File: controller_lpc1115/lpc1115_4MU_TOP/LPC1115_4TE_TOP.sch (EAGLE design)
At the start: 102 parts, among them P2 ISP, Q1 BC856, Q2 BCP52, Q3 BC847C, U1 LPC1115FBD48, U2 BD9G101, U3 XO32 12MHz

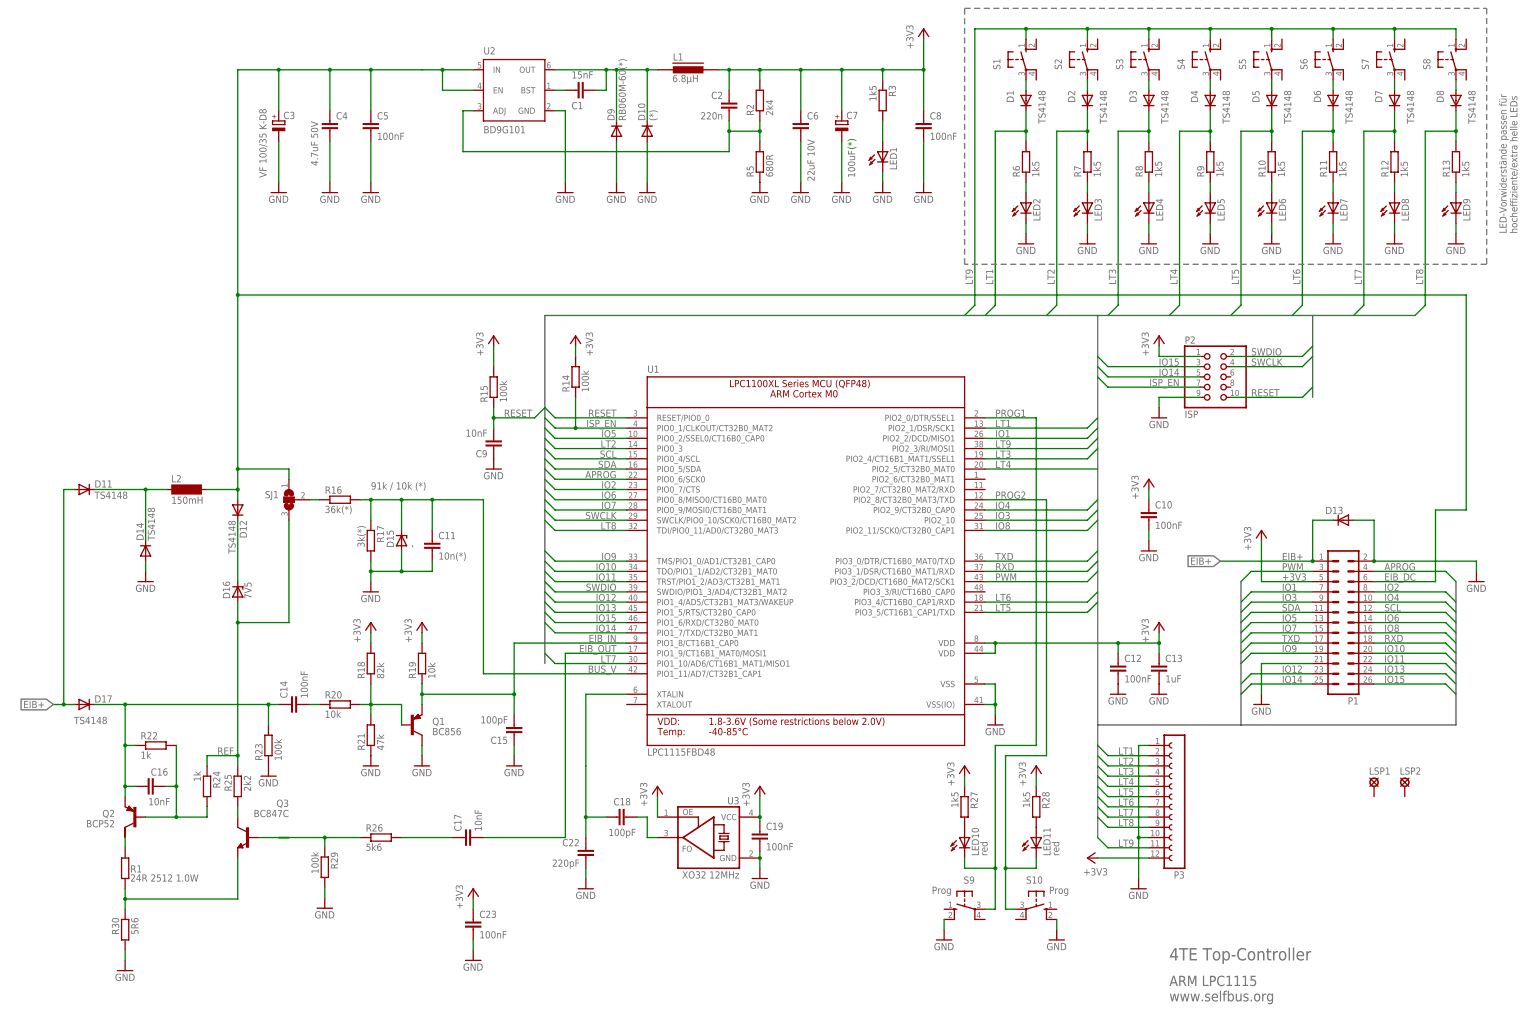
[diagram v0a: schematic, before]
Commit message: [ctrl_4MU_TOP] - intermediate status of re-routing
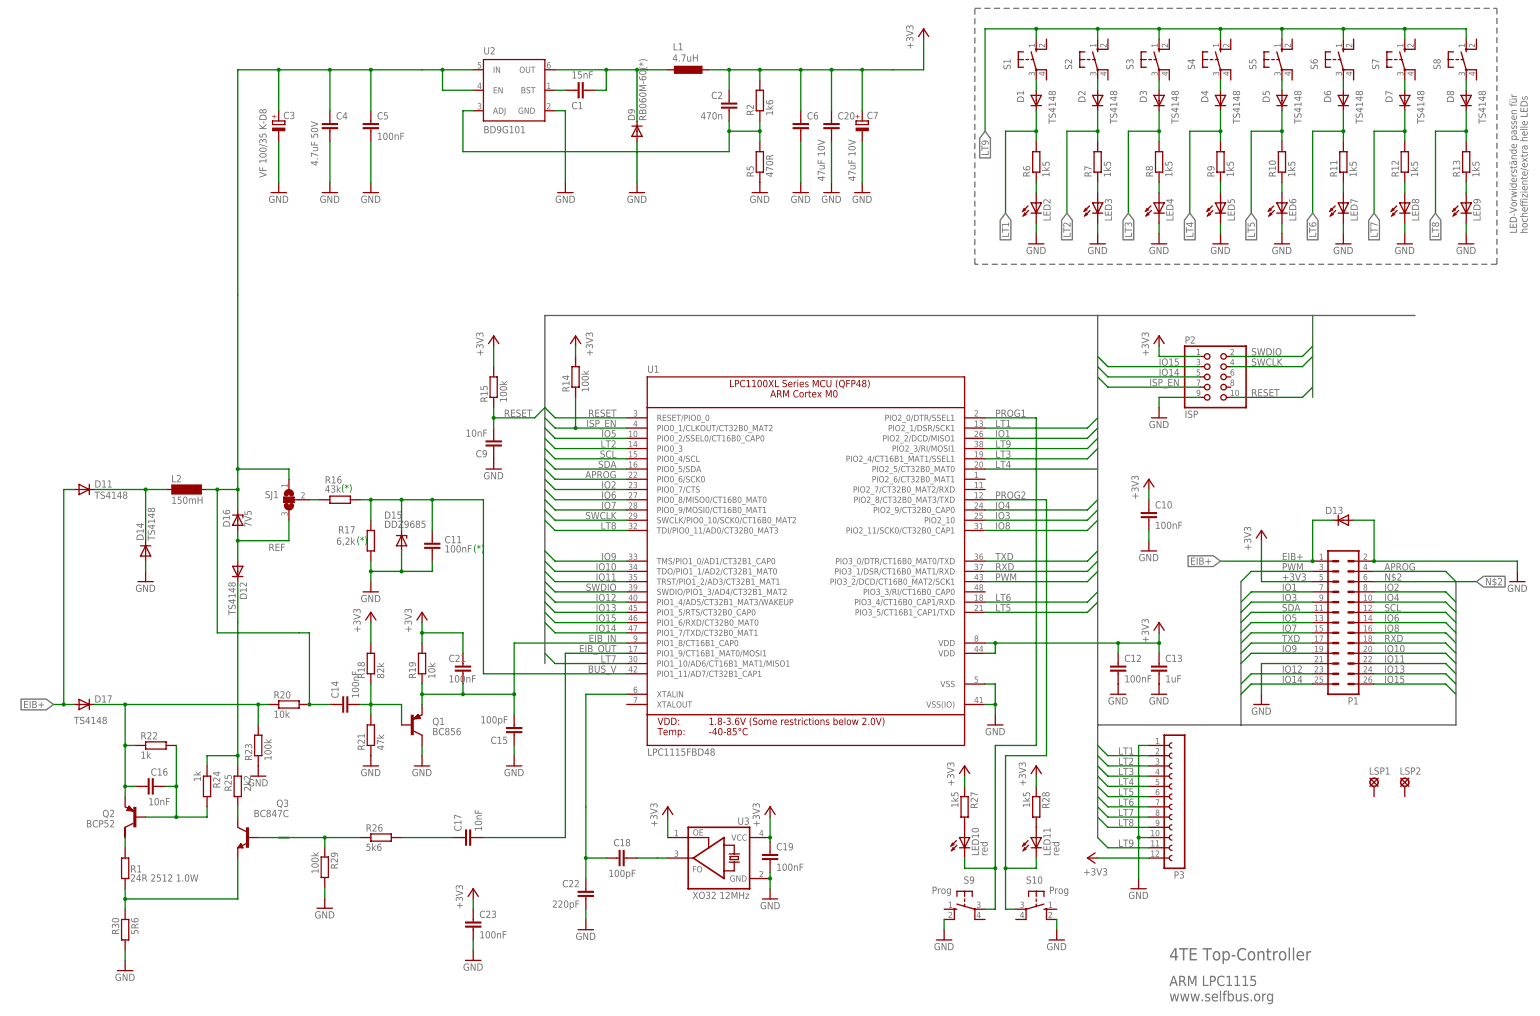
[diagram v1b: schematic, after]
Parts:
- removed C8: 100nF, rcl:C-EUC0805
- removed D10: (*), diode:DIODE-SMB
- removed LED1: (no value), led:LEDSMT1206
- removed R3: 1k5, rcl:R-EU_R0805
- added C20: 47uF 10V, rcl:C-EUC1206
- added C21: 100nF, rcl:C-EUC0805
- C11: value 10n(*) -> 100nF
- C2: value 220n -> 470n
- C6: value 22uF 10V -> 47uF 10V
- D15: value - -> DDZ9685
- L1: value 6.8µH -> 4.7uH; device Stefan_selfbus:IND_FASTRON_1616FPSB -> rcl:L-EUL4532P
- R1: device rcl:R-EU_R0805 -> rcl:R-EU_R2512
- R16: value 36k(*) -> 43k
- R17: value 3k(*) -> 6,2k
- R2: value 2k4 -> 1k6
- R5: value 680R -> 470R
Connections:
- net N$22 renamed XTALIN
- removed net N$13: LED1.A, R3.2
- removed net N$9: D12.C, D16.C
- new net N$70: D12.C, R24.1, R25.2
- net +3V3: now also C20.1, C21.2; no longer C8.1, R3.1
- net DRAIN: now also R20.1; no longer C14.1
- net EIB_DC: now also C14.1, D16.C, R20.2; no longer D12.A, P1.6
- net EIB_IN: now also C21.1
- net GND: now also C20.2; no longer C8.2, D10.A, LED1.C
- net LX: no longer D10.C
- net N$14: now also C14.2; no longer R20.2
- net N$2: now also P1.6; no longer C14.2, R20.1
- net REF: now also D12.A; no longer R24.1, R25.2
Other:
- note added: "D13 mit SMAJ40AC nur dann notwendig, wenn nicht näher EIB Steckverbinder eine vorhanden ist."
- note removed: "0,76mA"
- note removed: "91k / 10k (*)"
- note removed: "D13 mit SMAJ40C nur dann notwendig, wenn nicht näher EIB Steckverbinder eine vorhanden ist."
- note removed: "Fastron 1616FPS 6,8µ"
- note removed: "Power LED (LED4+R20) ist optional"
- moved on the sheet: C14, C18, C19, C22, C7, D1, D12, D16, D2, D3, D4, D5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

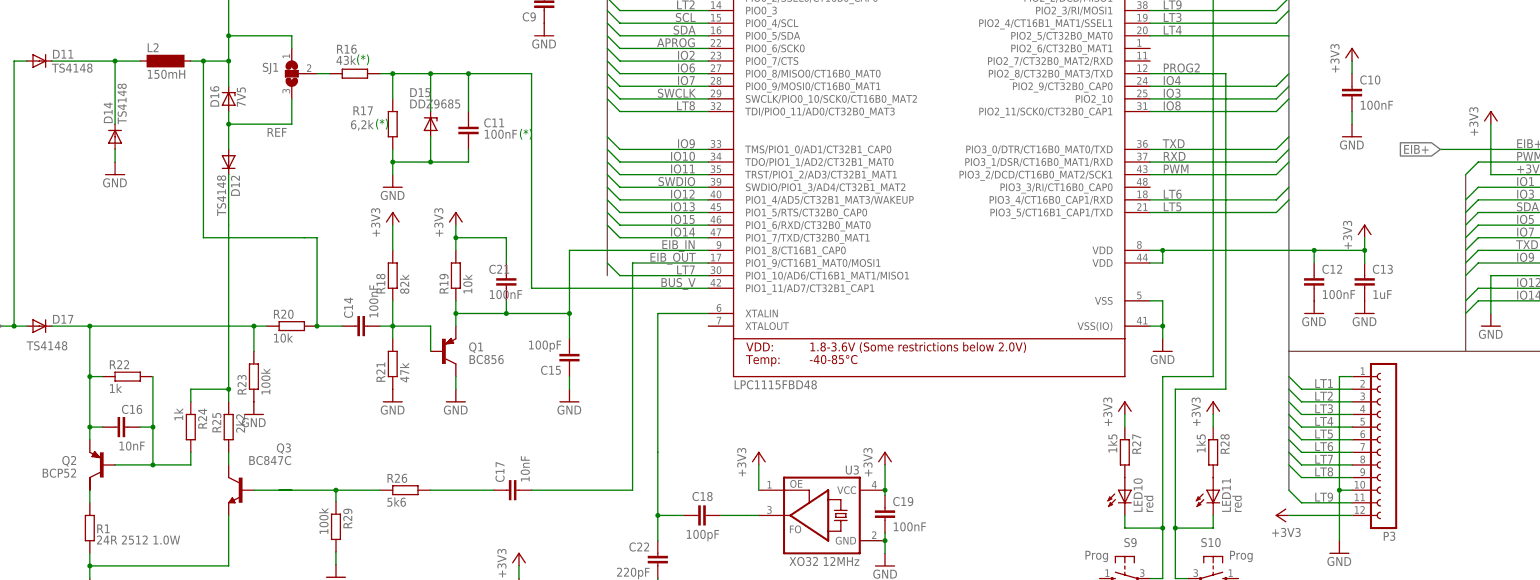
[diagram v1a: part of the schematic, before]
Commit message: [ctrl_4MU_TOP] - intermediate status of re-routing
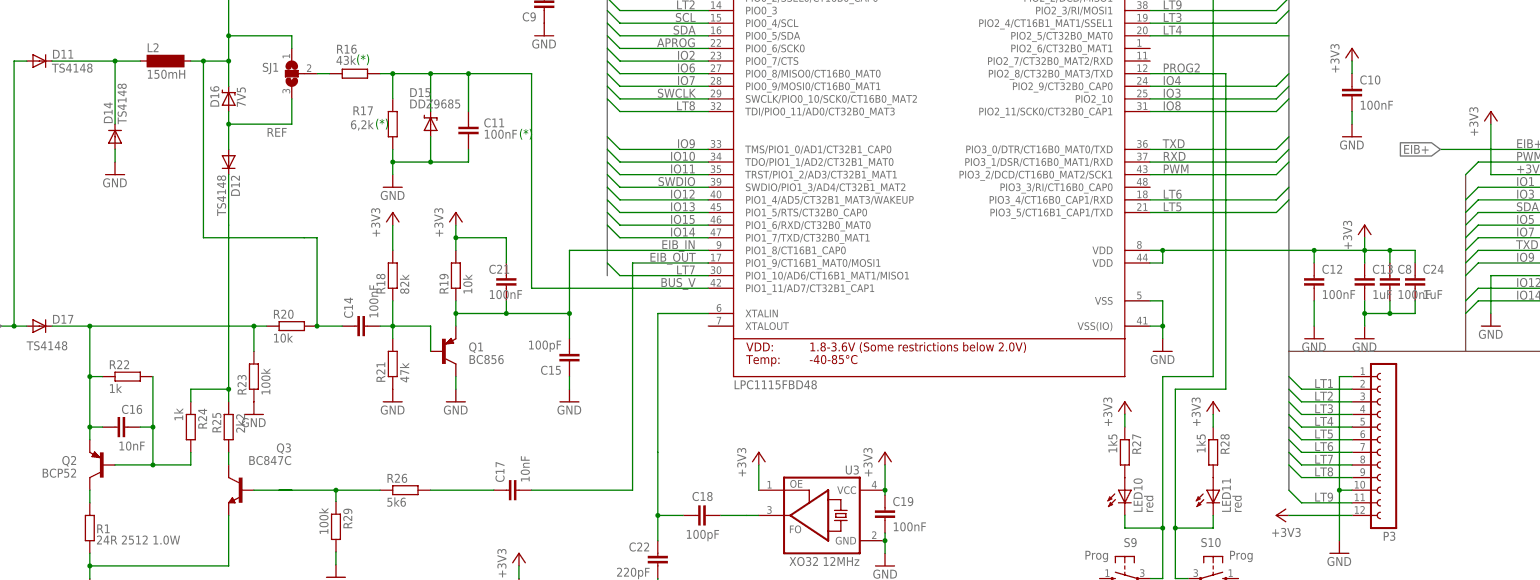
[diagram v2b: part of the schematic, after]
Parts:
- added C24: 1uF, rcl:C-EUC0805
- added C8: 100nF, rcl:C-EUC0805
- D15, D16: device diode:ZENER-DIODESOT23 -> Diode_for_Selfbus-Projects:DIODE-ZENERSOD-123
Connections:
- net +3V3: now also C24.1, C8.1
- net GND: now also C24.2, C8.2
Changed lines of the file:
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@@
 <part name="C12" library="rcl" library_urn="urn:adsk.eagle:library:334" deviceset="C-EU" device="C0805" package3d_urn="urn:adsk.eagle:package:23617/2" value="100nF"/>
 <part name="GND29" library="supply1" deviceset="GND" device=""/>
-<part name="Q2" library="transistor-pnp" deviceset="FZT753SMD" device="" value="BCP52"/>
+<part name="Q2" library="transistor-pnp" library_urn="urn:adsk.eagle:library:399" deviceset="FZT753SMD" device="" package3d_urn="urn:adsk.eagle:package:29214/2" value="BCP52"/>
 <part name="Q1" library="transistor-pnp" deviceset="BC856*" device="SMD" technology="B" value="BC856"/>
 <part name="U2" library="Stefan_selfbus" deviceset="BD9G101G" device="BD9G101G-SOT23-6MOD" value="BD9G101"/>
@@
 <part name="LED9" library="led" deviceset="LED" device="SMT1206"/>
 <part name="GND20" library="supply1" deviceset="GND" device=""/>
-<part name="P3" library="con-lsta" deviceset="FE12-1" device=""/>
+<part name="P3" library="con-lsta" deviceset="FE12-1" device="" package3d_urn="urn:adsk.eagle:package:8193/1"/>
 <part name="GND40" library="supply1" deviceset="GND" device=""/>
 <part name="+3V315" library="supply1" deviceset="+3V3" device=""/>
@@
 <part name="C7" library="rcl" deviceset="CPOL-EU" device="ESMD-D" value="100uF"/>
 <part name="GND10" library="supply1" deviceset="GND" device=""/>
-<part name="D16" library="diode" deviceset="ZENER-DIODE" device="SOT23" value="7V5"/>
-<part name="D15" library="diode" deviceset="ZENER-DIODE" device="SOT23" value="DDZ9685"/>
+<part name="D16" library="Diode_for_Selfbus-Projects" deviceset="DIODE-ZENER" device="SOD-123" package3d_urn="urn:adsk.eagle:package:40015434/2" value="7V5"/>
+<part name="D15" library="Diode_for_Selfbus-Projects" deviceset="DIODE-ZENER" device="SOD-123" package3d_urn="urn:adsk.eagle:package:40015434/2" value="DDZ9685"/>
 <part name="R1" library="rcl" library_urn="urn:adsk.eagle:library:334" deviceset="R-EU_" device="R2512" package3d_urn="urn:adsk.eagle:package:23545/2" value="24R  2512 1.0W"/>
 <part name="C20" library="rcl" library_urn="urn:adsk.eagle:library:334" deviceset="C-EU" device="C1206" package3d_urn="urn:adsk.eagle:package:23618/2" value="47uF 10V"/>
 <part name="GND4" library="supply1" deviceset="GND" device=""/>
 <part name="C21" library="rcl" library_urn="urn:adsk.eagle:library:334" deviceset="C-EU" device="C0805" package3d_urn="urn:adsk.eagle:package:23617/2" value="100nF"/>
+<part name="C8" library="rcl" library_urn="urn:adsk.eagle:library:334" deviceset="C-EU" device="C0805" package3d_urn="urn:adsk.eagle:package:23617/2" value="100nF"/>
+<part name="C24" library="rcl" library_urn="urn:adsk.eagle:library:334" deviceset="C-EU" device="C0805" package3d_urn="urn:adsk.eagle:package:23617/2" value="1uF"/>
 </parts>
 <sheets>
@@
 <attribute name="VALUE" x="165.1" y="50.8" size="1.778" layer="96" rot="R90"/>
 </instance>
-<instance part="GND27" gate="1" x="279.4" y="83.82" smashed="yes">
-<attribute name="VALUE" x="276.86" y="81.28" size="1.778" layer="96"/>
-</instance>
-<instance part="GND28" gate="1" x="289.56" y="83.82" smashed="yes">
-<attribute name="VALUE" x="287.02" y="81.28" size="1.778" layer="96"/>
+<instance part="GND27" gate="1" x="279.4" y="78.74" smashed="yes">
+<attribute name="VALUE" x="276.86" y="76.2" size="1.778" layer="96"/>
+</instance>
+<instance part="GND28" gate="1" x="289.56" y="78.74" smashed="yes">
+<attribute name="VALUE" x="287.02" y="76.2" size="1.778" layer="96"/>
 </instance>
 <instance part="GND2" gate="1" x="83.82" y="208.28" smashed="yes">
@@
 <attribute name="NAME" x="113.284" y="91.821" size="1.778" layer="95"/>
 <attribute name="VALUE" x="113.284" y="86.741" size="1.778" layer="96"/>
+</instance>
+<instance part="C8" gate="G$1" x="294.64" y="91.44" smashed="yes">
+<attribute name="NAME" x="296.164" y="91.821" size="1.778" layer="95"/>
+<attribute name="VALUE" x="296.164" y="86.741" size="1.778" layer="96"/>
+</instance>
+<instance part="C24" gate="G$1" x="299.72" y="91.44" smashed="yes">
+<attribute name="NAME" x="301.244" y="91.821" size="1.778" layer="95"/>
+<attribute name="VALUE" x="301.244" y="86.741" size="1.778" layer="96"/>
 </instance>
 </instances>
@@
 <pinref part="C12" gate="G$1" pin="2"/>
 <pinref part="GND27" gate="1" pin="GND"/>
+<wire x1="279.4" y1="81.28" x2="279.4" y2="86.36" width="0.1524" layer="91"/>
 </segment>
 <segment>
 <pinref part="C13" gate="G$1" pin="2"/>
 <pinref part="GND28" gate="1" pin="GND"/>
+<wire x1="289.56" y1="81.28" x2="289.56" y2="83.82" width="0.1524" layer="91"/>
+<wire x1="289.56" y1="83.82" x2="289.56" y2="86.36" width="0.1524" layer="91"/>
+<wire x1="289.56" y1="83.82" x2="294.64" y2="83.82" width="0.1524" layer="91"/>
+<junction x="289.56" y="83.82"/>
+<pinref part="C8" gate="G$1" pin="2"/>
+<wire x1="294.64" y1="83.82" x2="294.64" y2="86.36" width="0.1524" layer="91"/>
+<wire x1="294.64" y1="83.82" x2="299.72" y2="83.82" width="0.1524" layer="91"/>
+<junction x="294.64" y="83.82"/>
+<pinref part="C24" gate="G$1" pin="2"/>
+<wire x1="299.72" y1="83.82" x2="299.72" y2="86.36" width="0.1524" layer="91"/>
 </segment>
 <segment>
@@
 <pinref part="U1" gate="G$1" pin="VDD@2"/>
 <wire x1="246.38" y1="93.98" x2="248.92" y2="93.98" width="0.1524" layer="91"/>
-</segment>
-<segment>
+<wire x1="289.56" y1="96.52" x2="294.64" y2="96.52" width="0.1524" layer="91"/>
+<pinref part="C8" gate="G$1" pin="1"/>
+<wire x1="294.64" y1="96.52" x2="294.64" y2="93.98" width="0.1524" layer="91"/>
+<wire x1="294.64" y1="96.52" x2="299.72" y2="96.52" width="0.1524" layer="91"/>
+<junction x="294.64" y="96.52"/>
+<pinref part="C24" gate="G$1" pin="1"/>
+<wire x1="299.72" y1="96.52" x2="299.72" y2="93.98" width="0.1524" layer="91"/>
+</segment>
+<segment>
